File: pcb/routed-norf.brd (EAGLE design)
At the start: 30.5 x 30.5 mm, 84 parts, among them U2 CC430F5137IRGZR, X1 CRYSTALS-NOGND-IQXC-25

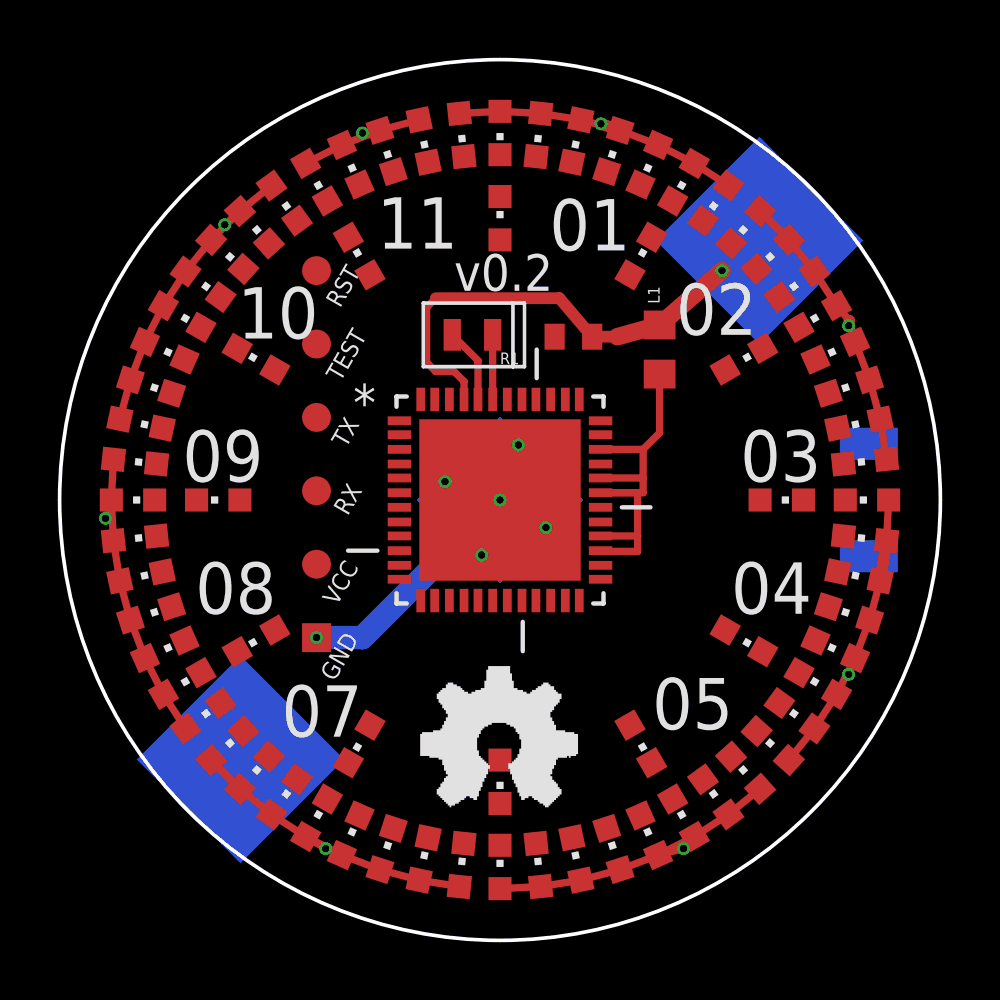
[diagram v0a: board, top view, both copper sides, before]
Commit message: routed version of the no-rf variant, with 1 square inch of board area
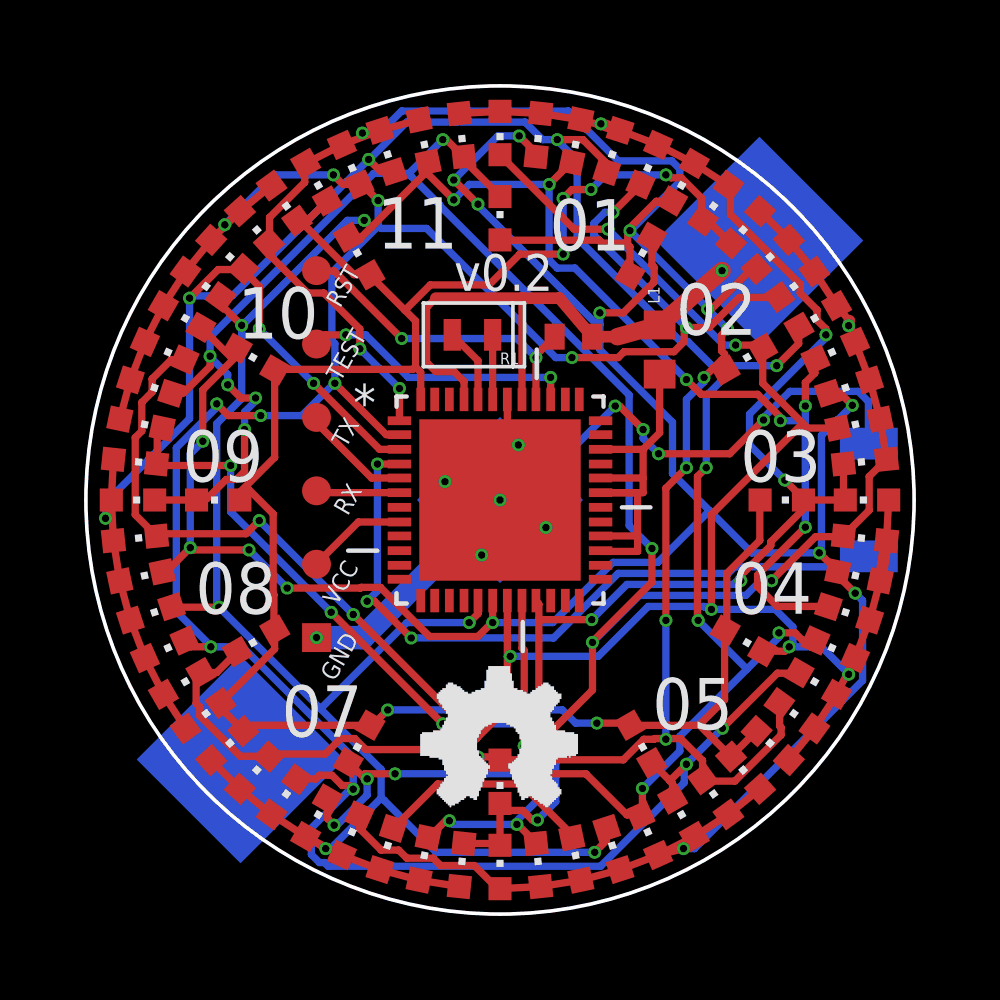
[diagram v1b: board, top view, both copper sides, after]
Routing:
- net B6: track 10.6 -> 101.3 mm, vias 1 -> 13
- net B5: track 10.5 -> 99.2 mm, vias 1 -> 15
- net B3: track 10.8 -> 97.4 mm, vias 1 -> 13
- net B7: track 4.84 -> 90.1 mm, vias 1 -> 12
- net B4: track 10.7 -> 93.1 mm, vias 1 -> 12
- net B1: track 10.1 -> 86.7 mm, vias 1 -> 12
- net B2: track 10.5 -> 86.1 mm, vias 1 -> 8
- net B8: track 0.00 -> 73.5 mm, vias 0 -> 6
- net B0: track 10.6 -> 70.3 mm, vias 1 -> 10
- net BUTTON: track 0.00 -> 24.7 mm, vias 0 -> 3
- net GND: track 21.2 -> 42.8 mm, vias 6 -> 10
- net BSL_RST: track 0.00 -> 11.3 mm, vias 0 -> 2
- net BSL_TEST: track 0.00 -> 9.61 mm, vias 0 -> 2
- net VCC: track 15.9 -> 21.1 mm
- net BSL_TX: track 0.00 -> 3.85 mm
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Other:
- board size 30.5 x 30.5 mm -> 28.7 x 28.7 mm

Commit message: as ordered from dirtypcb
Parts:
- added JP1: (no value), adafruit:1X06-BIGLOCK
- moved TP1 1.45 mm to (19.9, 19.5)
- moved TP3 1.45 mm to (19.9, 24.6)
- moved TP5 1.45 mm to (19.9, 29.7)
- moved TP4 1.17 mm to (19.3, 27.1)
- moved TP6 1.17 mm to (19.3, 32.2)
- moved TP2 1.17 mm to (19.3, 22.0)
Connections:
- net BSL_RST: now also JP1.6
- net BSL_RX: now also JP1.3
- net BSL_TEST: now also JP1.5
- net BSL_TX: now also JP1.4
- net BSL_VCC: now also JP1.2
- net GND: now also JP1.1
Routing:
- net B1: track 86.7 -> 76.2 mm, vias 12 -> 9
- net B6: track 101.3 -> 92.7 mm, vias 13 -> 11
- net B3: track 97.4 -> 88.9 mm, vias 13 -> 11
- net B2: track 86.1 -> 93.9 mm, vias 8 -> 10
- net GND: track 42.8 -> 50.3 mm, vias 10 -> 9
- net B0: track 70.3 -> 75.6 mm, vias 10 -> 7
- net BUTTON: track 24.7 -> 21.3 mm
- net B7: track 90.1 -> 92.1 mm, vias 12 -> 8
- net B8: track 73.5 -> 75.5 mm
- net BSL_RX: track 2.90 -> 3.70 mm
- net BSL_VCC: track 3.48 -> 4.15 mm
- net BSL_TX: track 3.85 -> 3.21 mm
- net B5: track 99.2 -> 99.7 mm, vias 15 -> 14
- net B4: track 93.1 -> 92.6 mm, vias 12 -> 10
- net BSL_TEST: track 9.61 -> 9.26 mm, vias 2 -> 1
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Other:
- board text added: "https://trmm.net/"
